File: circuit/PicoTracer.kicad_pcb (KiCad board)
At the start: 2 copper layers, 23 parts, among them J1 Conn_01x04_Socket, J10 Conn_01x02_Socket, J2 Conn_01x04_Socket, J3 Conn_01x02_Socket, J4 Conn_02x20_Top_Bottom, J5 Conn_02x20_Top_Bottom, J6 Conn_01x04_Socket, J7 8P8C, J9 Conn_01x02_Socket, SW1 SW_Push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

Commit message: 配線途中
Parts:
- moved Togle_SW1 58.9 mm to (183.4, 121.2)
- moved Togle_SW2 57.7 mm to (124.6, 121.2)
- moved U3 13.5 mm to (171.5, 69.8)
- moved U2 12.7 mm to (171.6, 83.2)
- moved J2 3.13 mm to (138.0, 126.9)
- moved J1 2.36 mm to (158.7, 126.9)
- moved R1 1.27 mm to (155.1, 115.7)
- moved R2 1.27 mm to (141.9, 115.7)
- moved Left1 0.62 mm to (115.0, 105.7)
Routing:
- net GND_12V: track 0.00 -> 105.3 mm
- net Net-(Left1-VMOT): track 0.00 -> 93.5 mm, vias 0 -> 1
- net Curve_Sensor: track 0.00 -> 84.2 mm
- net Net-(J4-Pin_22): track 0.00 -> 61.0 mm
- net GND_5V: track 0.00 -> 60.7 mm
- net +12V: track 0.00 -> 40.0 mm
- net Net-(U2-CH1): track 0.00 -> 39.2 mm
- net Net-(U2-CH0): track 0.00 -> 36.7 mm
- net Left_Direction: track 0.00 -> 32.0 mm
- net Net-(U3-CH1): track 0.00 -> 30.1 mm
- net Net-(J2-Pin_1): track 0.00 -> 28.6 mm
- net Net-(J2-Pin_2): track 0.00 -> 28.6 mm
- net Net-(J2-Pin_3): track 0.00 -> 28.6 mm
- net Net-(J2-Pin_4): track 0.00 -> 28.6 mm
- net Left_Step: track 0.00 -> 28.4 mm
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
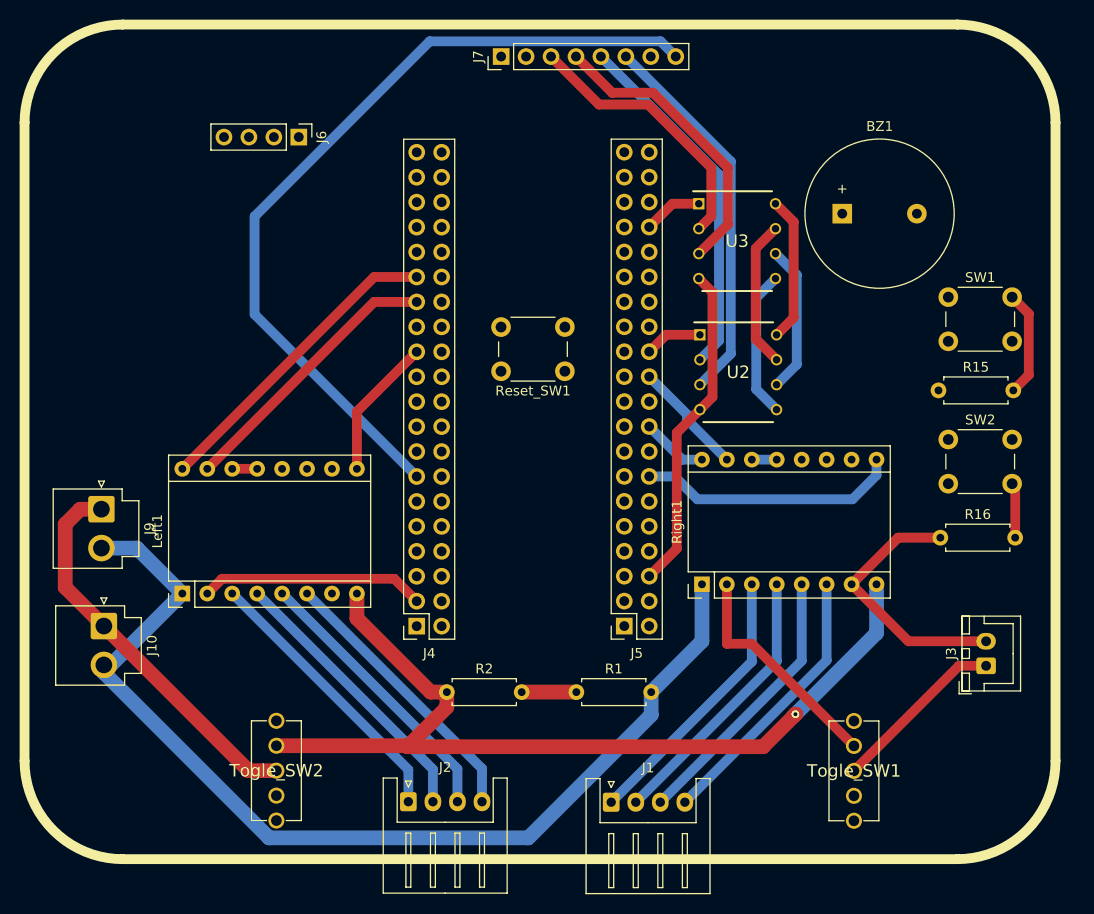
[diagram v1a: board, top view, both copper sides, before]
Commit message: 配線図完成、回路図スイッチの配線位置変更
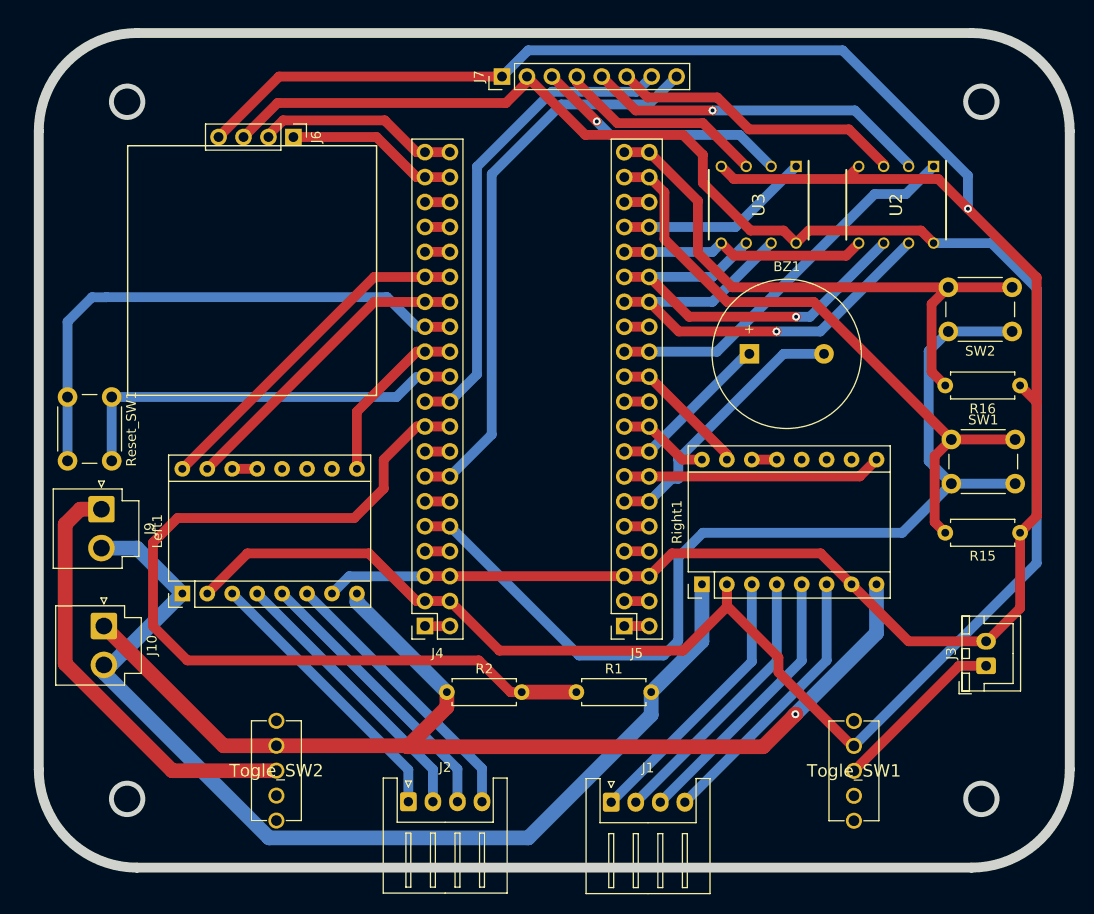
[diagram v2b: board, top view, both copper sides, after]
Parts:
- moved Reset_SW1 46.2 mm to (107.8, 85.7), turned to -90 degrees
- moved U2 23.4 mm to (187.7, 66.1), turned to -90 degrees
- moved R16 17.5 mm to (200.3, 84.5), turned to 180 degrees
- moved BZ1 17.1 mm to (172.7, 81.3)
- moved R15 16.7 mm to (200.3, 99.5), turned to 180 degrees
- moved SW1 14.5 mm to (193.3, 90.0)
- moved SW2 12.8 mm to (199.5, 79.0), turned to 180 degrees
- moved U3 4.31 mm to (173.7, 66.1), turned to -90 degrees
- moved J7 2.04 mm to (147.5, 53.0)
- moved J4 0.84 mm to (139.7, 109.0)
- moved J6 0.55 mm to (126.3, 59.2)
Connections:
- J10 pad 1: +12V -> Net-(J10-Pin_1)
- J4 pad 1: unconnected-(J4-Pin_1-Pad1) -> Net-(J4-Pin_1)
- J4 pad 10: unconnected-(J4-Pin_10-Pad10) -> Goal_Sensor
- J4 pad 11: unconnected-(J4-Pin_11-Pad11) -> Net-(J4-Pin_11)
- J4 pad 12: unconnected-(J4-Pin_12-Pad12) -> Left_Enable
- J4 pad 13: unconnected-(J4-Pin_13-Pad13) -> Net-(J4-Pin_13)
- J4 pad 14: unconnected-(J4-Pin_14-Pad14) -> Left_Step
- J4 pad 15: unconnected-(J4-Pin_15-Pad15) -> Left_Direction
- J4 pad 16: unconnected-(J4-Pin_16-Pad16) -> Net-(J4-Pin_16)
- J4 pad 17: unconnected-(J4-Pin_17-Pad17) -> Net-(J4-Pin_17)
- J4 pad 18: unconnected-(J4-Pin_18-Pad18) -> Net-(J4-Pin_18)
- J4 pad 19: unconnected-(J4-Pin_19-Pad19) -> Net-(J4-Pin_19)
- J4 pad 2: unconnected-(J4-Pin_2-Pad2) -> Net-(J4-Pin_2)
- J4 pad 20: unconnected-(J4-Pin_20-Pad20) -> Net-(J4-Pin_20)
- J4 pad 21: unconnected-(J4-Pin_21-Pad21) -> Net-(J4-Pin_1)
- J4 pad 22: Net-(J4-Pin_22) -> Net-(J4-Pin_2)
- J4 pad 24: unconnected-(J4-Pin_24-Pad24) -> Net-(J4-Pin_24)
- J4 pad 26: unconnected-(J4-Pin_26-Pad26) -> Net-(J4-Pin_26)
- J4 pad 28: unconnected-(J4-Pin_28-Pad28) -> Net-(J4-Pin_28)
- J4 pad 3: unconnected-(J4-Pin_3-Pad3) -> GND_5V
- J4 pad 31: Net-(J4-Pin_31) -> Net-(J4-Pin_11)
- J4 pad 33: Net-(J4-Pin_33) -> Net-(J4-Pin_13)
- J4 pad 36: unconnected-(J4-Pin_36-Pad36) -> Net-(J4-Pin_16)
- J4 pad 37: unconnected-(J4-Pin_37-Pad37) -> Net-(J4-Pin_17)
- J4 pad 38: unconnected-(J4-Pin_38-Pad38) -> Net-(J4-Pin_18)
- J4 pad 39: Net-(J4-Pin_39) -> Net-(J4-Pin_19)
- J4 pad 4: unconnected-(J4-Pin_4-Pad4) -> Net-(J4-Pin_24)
- J4 pad 40: Net-(J4-Pin_40) -> Net-(J4-Pin_20)
- J4 pad 5: unconnected-(J4-Pin_5-Pad5) -> 3.3V
- J4 pad 6: unconnected-(J4-Pin_6-Pad6) -> Net-(J4-Pin_26)
- J4 pad 7: unconnected-(J4-Pin_7-Pad7) -> Curve_Sensor
- J4 pad 8: unconnected-(J4-Pin_8-Pad8) -> Net-(J4-Pin_28)
- J4 pad 9: unconnected-(J4-Pin_9-Pad9) -> Net-(J4-Pin_29)
- J5 pad 1: unconnected-(J5-Pin_1-Pad1) -> Net-(J5-Pin_1)
- J5 pad 10: unconnected-(J5-Pin_10-Pad10) -> Net-(J5-Pin_10)
- J5 pad 13: unconnected-(J5-Pin_13-Pad13) -> Net-(J5-Pin_13)
- J5 pad 18: unconnected-(J5-Pin_18-Pad18) -> Net-(J5-Pin_18)
- J5 pad 2: unconnected-(J5-Pin_2-Pad2) -> Net-(J5-Pin_2)
- J5 pad 21: unconnected-(J5-Pin_21-Pad21) -> Net-(J5-Pin_1)
- J5 pad 22: unconnected-(J5-Pin_22-Pad22) -> Net-(J5-Pin_2)
- J5 pad 23: unconnected-(J5-Pin_23-Pad23) -> GND_5V
- J5 pad 24: unconnected-(J5-Pin_24-Pad24) -> Net-(J5-Pin_24)
- J5 pad 25: unconnected-(J5-Pin_25-Pad25) -> Net-(J5-Pin_25)
- J5 pad 26: unconnected-(J5-Pin_26-Pad26) -> Net-(BZ1--)
- J5 pad 27: unconnected-(J5-Pin_27-Pad27) -> Right_Enable
- J5 pad 28: unconnected-(J5-Pin_28-Pad28) -> Net-(BZ1-+)
- J5 pad 29: unconnected-(J5-Pin_29-Pad29) -> Right_Direction
- J5 pad 30: unconnected-(J5-Pin_30-Pad30) -> Net-(J5-Pin_10)
- J5 pad 31: unconnected-(J5-Pin_31-Pad31) -> Right_Step
- J5 pad 32: unconnected-(J5-Pin_32-Pad32) -> Sel1
- J5 pad 33: unconnected-(J5-Pin_33-Pad33) -> Net-(J5-Pin_13)
- J5 pad 34: unconnected-(J5-Pin_34-Pad34) -> Clock
- J5 pad 35: unconnected-(J5-Pin_35-Pad35) -> Dout
- J5 pad 36: unconnected-(J5-Pin_36-Pad36) -> Din
- J5 pad 37: unconnected-(J5-Pin_37-Pad37) -> Sel2
- J5 pad 38: unconnected-(J5-Pin_38-Pad38) -> Net-(J5-Pin_18)
- J5 pad 39: unconnected-(J5-Pin_39-Pad39) -> Net-(J5-Pin_19)
- J5 pad 4: unconnected-(J5-Pin_4-Pad4) -> Net-(J5-Pin_24)
- J5 pad 40: unconnected-(J5-Pin_40-Pad40) -> Net-(J5-Pin_20)
- J5 pad 5: unconnected-(J5-Pin_5-Pad5) -> Net-(J5-Pin_25)
- J6 pad 1: Net-(J4-Pin_39) -> Net-(J4-Pin_19)
- J6 pad 2: Net-(J4-Pin_40) -> Net-(J4-Pin_20)
- J6 pad 3: Net-(J4-Pin_22) -> Net-(J4-Pin_2)
- J7 pad 2: Net-(J4-Pin_22) -> Net-(J4-Pin_2)
- Left1 pad 2: Net-(J4-Pin_22) -> Net-(J4-Pin_2)
- Left1 pad 8: Net-(Left1-VMOT) -> Net-(J10-Pin_1)
- R2 pad 1: Net-(Left1-VMOT) -> Net-(J10-Pin_1)
- Reset_SW1 pad 1: Net-(J4-Pin_31) -> Net-(J4-Pin_11)
- Reset_SW1 pad 2: Net-(J4-Pin_33) -> Net-(J4-Pin_13)
- Right1 pad 2: Net-(J4-Pin_22) -> Net-(J4-Pin_2)
- Right1 pad 8: Net-(Left1-VMOT) -> Net-(J10-Pin_1)
- Togle_SW1 pad 1: Net-(J4-Pin_22) -> Net-(J4-Pin_2)
- Togle_SW2 pad 1: Net-(Left1-VMOT) -> Net-(J10-Pin_1)
- U2 pad 8: Net-(J4-Pin_22) -> Net-(J4-Pin_2)
- U3 pad 8: Net-(J4-Pin_22) -> Net-(J4-Pin_2)
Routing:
- net Net-(J4-Pin_2): track 0.00 -> 234.4 mm
- net GND_5V: track 60.7 -> 240.9 mm, vias 0 -> 1
- net Net-(J10-Pin_1): track 0.00 -> 115.1 mm, vias 0 -> 1
- net 3.3V: track 0.00 -> 101.6 mm
- net Net-(Left1-VMOT): track 93.5 -> 0.00 mm, vias 1 -> 0
- net Net-(J4-Pin_29): track 5.57 -> 91.3 mm
- net Net-(J4-Pin_22): track 61.0 -> 0.00 mm
- net Net-(J4-Pin_13): track 0.00 -> 54.6 mm
- net Net-(J5-Pin_20): track 5.63 -> 59.6 mm
- net Net-(J5-Pin_19): track 10.9 -> 64.3 mm
- net Goal_Sensor: track 0.00 -> 49.2 mm
- net Net-(J4-Pin_11): track 0.00 -> 41.0 mm
- net Clock: track 15.1 -> 48.8 mm, vias 0 -> 1
- net Sel1: track 5.87 -> 39.3 mm
- net Net-(BZ1--): track 0.00 -> 27.7 mm
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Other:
- board outline added: 105 x 85 mm
